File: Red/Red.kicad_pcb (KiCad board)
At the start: 4 copper layers, 64 x 100 mm, 67 parts, among them IC201 STM32G473CET6, J201 Conn_01x06, J501 USB_C_Receptacle, J502 Conn_01x10, J503 Conn_01x10, J701 Conn_01x03, J702 Conn_01x03, J703 Screw_Terminal_01x02, J704 Screw_Terminal_01x02, J801 Conn_01x02, Q701 DMG3414U, Q702 DMG3414U, Q703 DMG3414U, Q704 DMG3414U, Q705 DMG3414U, SW201 SW_Push, U201 MAX7375AXR805, U401 MPL115A1, U402 ICM-20948, U501 USBLC6-2SC6, U802 AZ1117-3.3, U803 AZ1117-5.0, Y201 SIT1533AI-H4-DCC-32.768E

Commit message: Made one library in the project folder with all symbols and footprints for easy sharing
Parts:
- J704: footprint my_library:2_pin_screw_terminal -> Red:2_pin_screw_terminal
- SW201: footprint my_library:SMD_Push_Switch -> Red:SMD_Push_Switch
- renumbered I601 to I1
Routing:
- net GND: track 154.3 -> 161.6 mm

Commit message: updated documentation and fixed a few minor erros
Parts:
- removed J701: Conn_01x03, my_library:WM4901-ND
- added e1: Conn_01x03, Red:WM4901-ND, F.Cu at (162.0, 104.5)
- D1: footprint my_library:LED_RGB_3.5mmx2.8mm -> Red:LED_RGB_3.5mmx2.8mm
- J702: footprint my_library:WM4901-ND -> Red:WM4901-ND
- J703: footprint my_library:2_pin_screw_terminal -> Red:2_pin_screw_terminal
- R706, R708: footprint my_library:dpak_back_isolated -> Red:dpak_back_isolated
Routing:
- net +3V3: track 57.9 -> 62.9 mm, vias 17 -> 19
- net GND: track 161.6 -> 165.4 mm
- net VBUS: track 16.6 -> 18.8 mm
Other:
- board text added: "3 amp Channel"
- board text added: "Arm For 3 Amp channels"
- board text added: "Cap for 3 Amp Channels"
- board text added: "IO Pins"
- board text added: "Power Pins"

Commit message: Post design review
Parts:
- removed the J201 at (120.2, 133.9)
- removed J501: USB_C_Receptacle, Connector_USB:USB_C_Receptacle_Amphenol_12401548E4-2A
- removed J502, J503: Conn_01x10, Connector_PinHeader_2.54mm:PinHeader_1x10_P2.54mm_Vertical
- removed JP101: Jumper_2_Bridged, digikey-kicad-library:PinHeader_1x2_P2.54mm
- removed the R301 at (129.2, 139.2)
- removed the R302 at (129.2, 137.3)
- removed the R303 at (129.2, 135.5)
- removed the R304 at (149.2, 135.8)
- removed the R305 at (149.2, 137.5)
- removed the R306 at (149.2, 139.2)
- removed R501, R502: 5k, Capacitor_SMD:C_0402_1005Metric
- removed R503, R504: 22, Capacitor_SMD:C_0402_1005Metric
- removed the U501 at (139.1, 138.3)
- added C801: 27pF, Capacitor_SMD:C_0402_1005Metric, F.Cu at (145.3, 141.5)
- added C802: 27pF, Capacitor_SMD:C_0402_1005Metric, F.Cu at (132.7, 141.6)
- added D801: D, Diode_SMD:D_SOD-323, F.Cu at (153.8, 139.6)
- added D802: LEDY, Diode_SMD:D_0603_1608Metric_Pad1.05x0.95mm_HandSolder, F.Cu at (147.9, 146.4)
- added D803: LEDG, Diode_SMD:D_0603_1608Metric_Pad1.05x0.95mm_HandSolder, F.Cu at (145.3, 146.4)
- added J701: Conn_01x06, Red:j-link_6_pin_needle, F.Cu at (122.4, 126.6)
- added J801: USB_C_Receptacle, Connector_USB:USB_C_Receptacle_Amphenol_12401548E4-2A, F.Cu at (139.0, 147.3)
- added J802: Conn_01x10, Connector_PinHeader_2.54mm:PinHeader_1x10_P2.54mm_Vertical, F.Cu at (162.0, 144.0)
- added J803: Conn_01x10, Connector_PinHeader_2.54mm:PinHeader_1x10_P2.54mm_Vertical, F.Cu at (115.8, 143.8)
- added R601: 270, Resistor_SMD:R_0402_1005Metric, F.Cu at (148.6, 133.8)
- added R602: 270, Resistor_SMD:R_0402_1005Metric, F.Cu at (148.6, 135.2)
- added R603: 270, Resistor_SMD:R_0402_1005Metric, F.Cu at (148.6, 136.7)
- added R604: 270, Resistor_SMD:R_0402_1005Metric, F.Cu at (128.5, 136.0)
- added R605: 270, Resistor_SMD:R_0402_1005Metric, F.Cu at (128.5, 134.7)
- added R606: 270, Resistor_SMD:R_0402_1005Metric, F.Cu at (128.5, 133.3)
- added R801: 5k, Capacitor_SMD:C_0402_1005Metric, F.Cu at (133.0, 144.9)
- added R802: 5k, Capacitor_SMD:C_0402_1005Metric, F.Cu at (133.0, 147.2)
- added R803: 27, Resistor_SMD:R_0402_1005Metric, F.Cu at (143.9, 140.3)
- added R804: 27, Resistor_SMD:R_0402_1005Metric, F.Cu at (134.1, 140.4)
- added R805: 10k, Resistor_SMD:R_0603_1608Metric_Pad1.05x0.95mm_HandSolder, F.Cu at (132.9, 134.2)
- added R806: 10k, Resistor_SMD:R_0603_1608Metric_Pad1.05x0.95mm_HandSolder, F.Cu at (132.9, 136.0)
- added R807: 10k, Resistor_SMD:R_0603_1608Metric_Pad1.05x0.95mm_HandSolder, F.Cu at (146.7, 129.6)
- added R808: 10k, Resistor_SMD:R_0603_1608Metric_Pad1.05x0.95mm_HandSolder, F.Cu at (146.7, 127.3)
- added R809: 270, Resistor_SMD:R_0402_1005Metric, F.Cu at (147.9, 149.6)
- added R810: 270, Resistor_SMD:R_0402_1005Metric, F.Cu at (145.3, 149.6)
- added TP701: TestPoint, Red:Test_Point_2.67x1.02mm, F.Cu at (119.7, 117.0)
- added TP702: TestPoint, Red:Test_Point_2.67x1.02mm, F.Cu at (134.4, 111.5)
- added TP703: TestPoint, Red:Test_Point_2.67x1.02mm, F.Cu at (119.7, 114.7)
- added TP704: TestPoint, Red:Test_Point_2.67x1.02mm, F.Cu at (132.2, 104.6)
- added TP705: TestPoint, Red:Test_Point_2.67x1.02mm, F.Cu at (128.7, 104.6)
- added TP706: TestPoint, Red:Test_Point_2.67x1.02mm, F.Cu at (123.6, 118.5)
- added U801: FT230XS, Package_SO:SSOP-16_3.9x4.9mm_P0.635mm, F.Cu at (138.9, 137.6)
- moved D602 29.3 mm to (124.6, 135.1), turned to 180 degrees
- moved D601 29.1 mm to (153.4, 135.1), turned to 0 degrees
- moved SW701 2.61 mm to (138.8, 129.7)
- moved C503 0.50 mm to (156.5, 132.1)
- renumbered C802 to C201, C803 to C202, C805 to C203, C806 to C204, C701 to C301, C401 to C501, C402 to C502, C403 to C503, C404 to C504, C405 to C505, C201 to C701, C202 to C702, C208 to C703, C204 to C704, C205 to C705, C206 to C706, C209 to C707, D1 to D601, D2 to D602, I1 to I401, IC201 to IC701, J801 to J201, J702 to J301, J703 to J302, J704 to J303, Q701 to Q301, Q702 to Q302, Q703 to Q303, Q704 to Q304, Q705 to Q305, R701 to R301, R702 to R302, R703 to R303, R704 to R304, R705 to R305, R706 to R306, R707 to R307, R708 to R308, R201 to R701, SW201 to SW701, U802 to U201, U803 to U202, U401 to U501, U402 to U502, U201 to U701, Y201 to Y701, e1 to e301
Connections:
- net /Microprocessor/MISO renamed /IOConnector/MISO
- net /Microprocessor/MOSI renamed /IOConnector/MOSI
- IC701 pad 31: /IOConnector/USART_TX -> /IOConnector/RXD
- IC701 pad 32: /IOConnector/USART_RX -> /IOConnector/TXD
- IC701 pad 33: /IOConnector/USB_D- -> /Microprocessor/USART_CTS
- IC701 pad 34: /IOConnector/USB_D+ -> /Microprocessor/USART_RTS
- IC701 pad 38: /Microprocessor/SWDCLK -> /Microprocessor/SWCLK
- IC701 pad 43: /IOConnector/D3 -> /Sensors/INT1
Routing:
- net /IOConnector/D3: track 31.8 -> 0.00 mm, vias 2 -> 0
- net /Microprocessor/SWDCLK: track 29.0 -> 0.00 mm, vias 1 -> 0
- net /Microprocessor/SWCLK: track 0.00 -> 28.2 mm, vias 0 -> 2
- net /IOConnector/USART_TX: track 27.3 -> 0.00 mm, vias 1 -> 0
- net /IOConnector/USART_RX: track 24.5 -> 0.00 mm, vias 1 -> 0
- net /Microprocessor/USART_RTS: track 0.00 -> 22.5 mm
- net /Microprocessor/USART_CTS: track 0.00 -> 21.9 mm, vias 0 -> 2
- net Net-(J801-PadS1): track 0.00 -> 21.5 mm
- net Net-(J501-PadS1): track 21.0 -> 0.00 mm
- net /IOConnector/TXD: track 0.00 -> 19.7 mm, vias 0 -> 2
- net /IOConnector/RXD: track 0.00 -> 18.3 mm
- net /IOConnector/USB_D-: track 16.2 -> 0.00 mm
- net /IOConnector/USB_D+: track 15.6 -> 0.00 mm
- net +3V3: track 62.9 -> 77.9 mm, vias 19 -> 28
- net /Microprocessor/NRST: track 53.1 -> 39.2 mm, vias 2 -> 0
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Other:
- board text added: "6 Pin SWD"
- board text added: "FTDI"
- board text added: "SWD"
- board text removed: "NRST"
- board text removed: "SWD Connection"
- board text removed: "SWDCLK"
- board text removed: "SWDIO"
- board text removed: "SWO"
- board text removed: "V_REF"

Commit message: Changed Silkscreen to accurately reflect pinout
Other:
- board text added: "MISO"
- board text added: "MOSI"
- board text added: "SCK"
- board text removed: "D3"
- board text removed: "RX"
- board text removed: "TX"

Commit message: Few minor silkscreen changes
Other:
- board text added: "QSLCK"
- board text added: "QSPI_0"
- board text added: "QSPI_1"
- board text added: "QSPI_2"
- board text added: "QSPI_3"
- board text added: "QSPI_CS"
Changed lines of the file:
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@@
   (general
     (thickness 1.6)
-    (drawings 140)
+    (drawings 146)
     (tracks 920)
     (zones 0)
@@
   (layers
     (0 F.Cu signal)
-    (1 3V3.Cu power)
-    (2 GND.Cu power)
+    (1 3V3.Cu power hide)
+    (2 GND.Cu power hide)
     (31 B.Cu signal)
     (33 F.Adhes user)
@@
     (at 123.6 118.5)
     (attr smd)
-    (fp_text reference TP706 (at 0 1.2) (layer F.SilkS)
+    (fp_text reference TP706 (at 2.1 0.1 90) (layer F.SilkS) hide
       (effects (font (size 0.5 0.5) (thickness 0.1)))
     )
@@
     (at 128.7 104.6)
     (attr smd)
-    (fp_text reference TP705 (at 0.01 -1.1) (layer F.SilkS)
+    (fp_text reference TP705 (at 0.01 1.2) (layer F.SilkS) hide
       (effects (font (size 0.5 0.5) (thickness 0.1)))
     )
@@
     (at 132.2 104.6)
     (attr smd)
-    (fp_text reference TP704 (at 0.01 -1.2) (layer F.SilkS)
+    (fp_text reference TP704 (at 1.95 0.1 90) (layer F.SilkS) hide
       (effects (font (size 0.5 0.5) (thickness 0.1)))
     )
@@
     (at 119.7 114.7)
     (attr smd)
-    (fp_text reference TP703 (at 0 1.1) (layer F.SilkS)
+    (fp_text reference TP703 (at -1.85 0.05 90) (layer F.SilkS) hide
       (effects (font (size 0.5 0.5) (thickness 0.1)))
     )
@@
     (at 134.4 111.5)
     (attr smd)
-    (fp_text reference TP702 (at 0 1) (layer F.SilkS)
+    (fp_text reference TP702 (at 2.15 -0.2 90) (layer F.SilkS) hide
       (effects (font (size 0.5 0.5) (thickness 0.1)))
     )
@@
     (at 119.7 117)
     (attr smd)
-    (fp_text reference TP701 (at 0 1.1) (layer F.SilkS)
+    (fp_text reference TP701 (at -1.85 0.25 90) (layer F.SilkS) hide
       (effects (font (size 0.5 0.5) (thickness 0.1)))
     )
@@
     )
   )
+  (gr_text "QSPI_3\n" (at 123.55 119.8) (layer F.SilkS)
+    (effects (font (size 0.5 0.5) (thickness 0.1)))
+  )
+  (gr_text "QSPI_CS\n" (at 134.45 112.7) (layer F.SilkS)
+    (effects (font (size 0.5 0.5) (thickness 0.1)))
+  )
+  (gr_text "QSPI_1\n" (at 132.15 103.45) (layer F.SilkS)
+    (effects (font (size 0.5 0.5) (thickness 0.1)))
+  )
+  (gr_text "QSPI_2\n\n" (at 128.75 103.9) (layer F.SilkS)
+    (effects (font (size 0.5 0.5) (thickness 0.1)))
+  )
+  (gr_text QSLCK (at 119.7 118.5) (layer F.SilkS)
+    (effects (font (size 0.5 0.5) (thickness 0.1)))
+  )
+  (gr_text "QSPI_0\n" (at 119.75 115.75) (layer F.SilkS)
+    (effects (font (size 0.5 0.5) (thickness 0.1)))
+  )
   (gr_line (start 118.3 138.8) (end 131 138.8) (layer Cmts.User) (width 0.15))

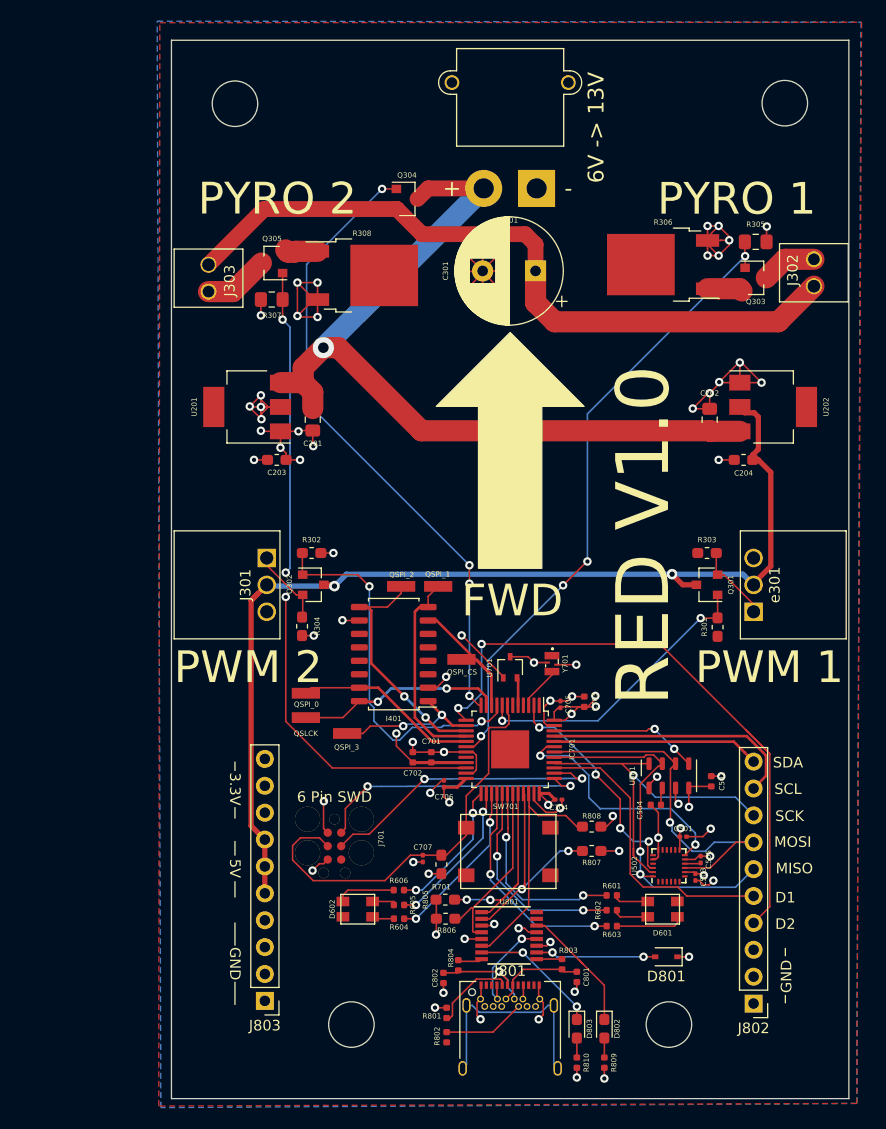
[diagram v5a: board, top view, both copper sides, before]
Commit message: Swapped USBC connector out for one that was available, minor Silkscreen tweaks
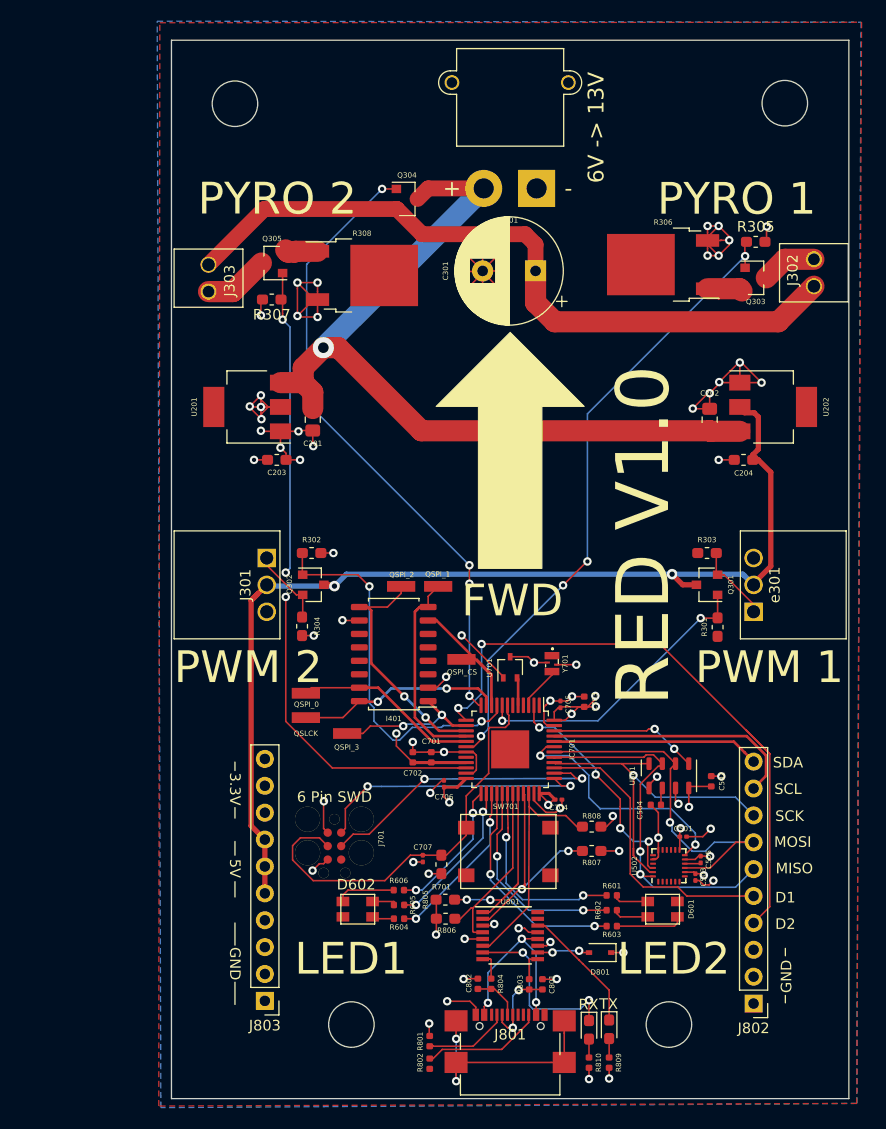
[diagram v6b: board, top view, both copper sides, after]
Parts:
- D602: footprint my_library:LED_RGB_3.5mmx2.8mm -> Red:LED_RGB_3.5mmx2.8mm
- J801: footprint Connector_USB:USB_C_Receptacle_Amphenol_12401548E4-2A -> Red:USB_C_Receptacle_USB4110
- R305, R307: footprint Resistor_SMD:R_0805_2012Metric_Pad1.15x1.40mm_HandSolder -> Resistor_SMD:R_0603_1608Metric_Pad1.05x0.95mm_HandSolder
- moved D801 6.26 mm to (147.5, 139.2)
- moved R803 3.64 mm to (140.8, 142.2)
- moved R804 3.56 mm to (137.2, 142.2)
- moved C801 3.32 mm to (142.1, 142.2), turned to 90 degrees
- moved C802 3.30 mm to (135.9, 142.2), turned to 90 degrees
- moved R801 3.11 mm to (131.4, 147.6)
- moved R802 2.97 mm to (131.4, 149.7)
- moved J801 1.45 mm to (139.0, 148.8)
- moved D803 1.15 mm to (146.4, 146.5)
- moved R810 1.15 mm to (146.4, 149.6)
- moved D802 0.45 mm to (148.3, 146.4)
- moved R809 0.45 mm to (148.3, 149.6)
- moved U801 0.10 mm to (139.0, 137.6)
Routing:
- net VBUS: track 11.3 -> 17.8 mm, vias 1 -> 3
- net Net-(D801-Pad2): track 11.4 -> 5.09 mm
- net /IOConnector/USBD+: track 10.2 -> 4.52 mm, vias 1 -> 0
- net Net-(D803-Pad1): track 12.3 -> 17.2 mm
- net Net-(J801-PadB5): track 7.80 -> 11.5 mm
- net GND: track 166.2 -> 163.5 mm, vias 55 -> 54
- net Net-(R804-Pad1): track 2.29 -> 3.37 mm
- net Net-(J801-PadS1): track 21.5 -> 22.3 mm, vias 0 -> 2
- net /IOConnector/USBD-: track 8.64 -> 9.21 mm, vias 0 -> 2
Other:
- board text added: "LED1"
- board text added: "LED2"
- board text added: "RX"
- board text added: "TX"

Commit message: Final Manufacturing Modifactions for Version 1.0
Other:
- rule pad_to_mask_clearance: 0.051 -> 0.05
- rule solder_mask_min_width: 0.25 -> 0.1
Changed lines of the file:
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@@
   (page A4)
   (layers
-    (0 F.Cu signal)
-    (1 3V3.Cu power)
-    (2 GND.Cu power)
-    (31 B.Cu signal)
-    (32 B.Adhes user)
-    (33 F.Adhes user)
-    (34 B.Paste user)
-    (35 F.Paste user)
-    (36 B.SilkS user)
-    (37 F.SilkS user)
-    (38 B.Mask user)
+    (0 F.Cu signal hide)
+    (1 3V3.Cu power hide)
+    (2 GND.Cu power hide)
+    (31 B.Cu signal hide)
+    (32 B.Adhes user hide)
+    (33 F.Adhes user hide)
+    (34 B.Paste user hide)
+    (35 F.Paste user hide)
+    (36 B.SilkS user hide)
+    (37 F.SilkS user hide)
+    (38 B.Mask user hide)
     (39 F.Mask user)
-    (40 Dwgs.User user)
-    (41 Cmts.User user)
-    (42 Eco1.User user)
-    (43 Eco2.User user)
-    (44 Edge.Cuts user)
-    (45 Margin user)
-    (46 B.CrtYd user)
-    (47 F.CrtYd user)
-    (48 B.Fab user)
+    (40 Dwgs.User user hide)
+    (41 Cmts.User user hide)
+    (42 Eco1.User user hide)
+    (43 Eco2.User user hide)
+    (44 Edge.Cuts user hide)
+    (45 Margin user hide)
+    (46 B.CrtYd user hide)
+    (47 F.CrtYd user hide)
+    (48 B.Fab user hide)
     (49 F.Fab user hide)
   )
@@
     (pad_size 4.3 4.3)
     (pad_drill 4.3)
-    (pad_to_mask_clearance 0.051)
-    (solder_mask_min_width 0.25)
+    (pad_to_mask_clearance 0.05)
+    (solder_mask_min_width 0.1)
     (aux_axis_origin 0 0)
     (grid_origin 119.4 121.4)
     (visible_elements 7FFFFFFF)
     (pcbplotparams
-      (layerselection 0x010a8_ffffffff)
+      (layerselection 0x010ff_ffffffff)
       (usegerberextensions false)
       (usegerberattributes false)
